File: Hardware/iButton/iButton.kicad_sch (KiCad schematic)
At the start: 29 parts, among them IC1 TSOP75338TR, J1 Conn_01x06, X1b1 PG-2.5-9.5-SM, X2b1 PG-2.5-8.0-SM, X3b1 PG-3.0-10.0-SM

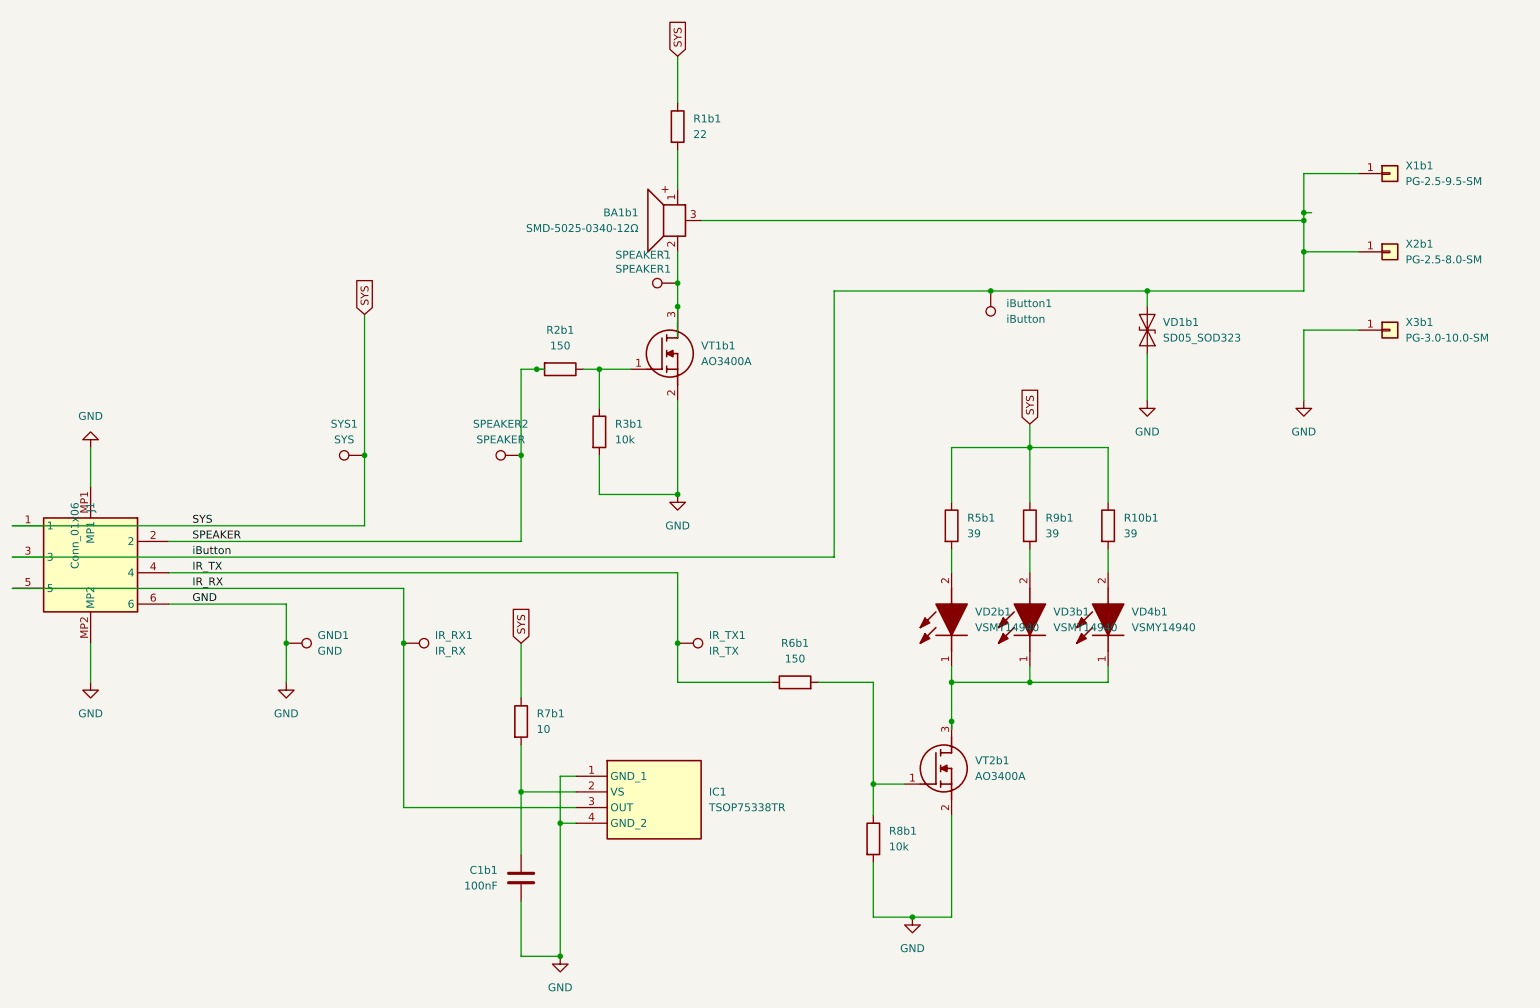
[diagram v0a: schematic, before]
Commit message: PCB: Re layout the iBTN board
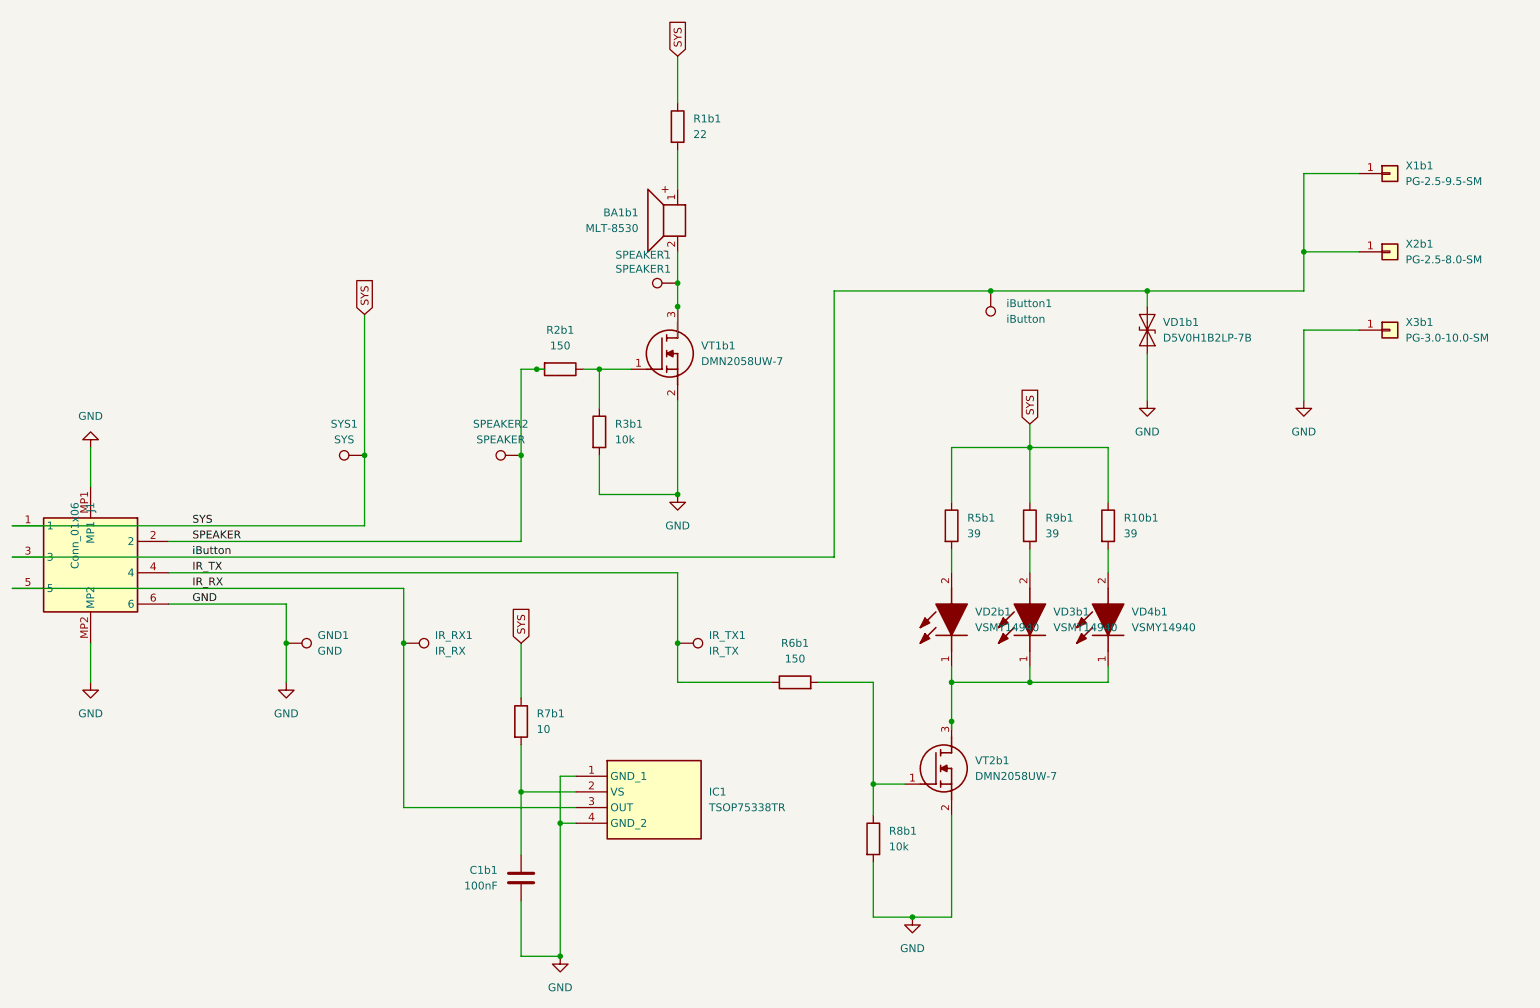
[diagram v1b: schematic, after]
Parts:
- BA1b1: value SMD-5025-0340-12Ω -> MLT-8530; footprint Library:BUZ-SMD_3P-L5.0-W5.0-BL -> Library:MLT8530
- GND1, IR_RX1, IR_TX1, SPEAKER1, SPEAKER2, SYS1, iButton1: footprint TestPoint:TestPoint_Pad_1.0x1.0mm -> TestPoint:TestPoint_Pad_D1.0mm
- VD1b1: value SD05_SOD323 -> D5V0H1B2LP-7B; footprint Diode_SMD:D_SOD-323 -> Library:D5V0H1B2LP7B
- VT1b1, VT2b1: value AO3400A -> DMN2058UW-7; footprint SOT95P280X125-3N -> Library:SOT65P210X110-3N
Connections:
- net iButton: no longer BA1b1.3
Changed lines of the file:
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@@
 	)
 	(junction
-		(at 228.6 50.8)
-		(diameter 0)
-		(color 0 0 0 0)
-	)
-	(junction
 		(at 107.95 149.86)
 		(diameter 0)
@@
 	)
 	(junction
-		(at 228.6 52.07)
-		(diameter 0)
-		(color 0 0 0 0)
-	)
-	(junction
 		(at 127 96.52)
 		(diameter 0)
@@
 	(wire
 		(pts
-			(xy 228.6 57.15) (xy 228.6 52.07)
+			(xy 228.6 44.45) (xy 228.6 57.15)
 		)
 		(stroke
@@
 	(wire
 		(pts
-			(xy 130.81 52.07) (xy 228.6 52.07)
-		)
-		(stroke
-			(width 0)
-			(type default)
-		)
-	)
-	(wire
-		(pts
 			(xy 101.6 162.56) (xy 101.6 171.45)
 		)
@@
 	(wire
 		(pts
-			(xy 228.6 52.07) (xy 228.6 50.8)
-		)
-		(stroke
-			(width 0)
-			(type default)
-		)
-	)
-	(wire
-		(pts
 			(xy 63.5 120.65) (xy 63.5 114.3)
 		)
@@
 	(wire
 		(pts
-			(xy 229.87 50.8) (xy 228.6 50.8)
-		)
-		(stroke
-			(width 0)
-			(type default)
-		)
-	)
-	(wire
-		(pts
 			(xy 101.6 137.16) (xy 101.6 144.78)
 		)
@@
 	(wire
 		(pts
-			(xy 228.6 44.45) (xy 228.6 50.8)
-		)
-		(stroke
-			(width 0)
-			(type default)
-		)
-	)
-	(wire
-		(pts
 			(xy 127 127) (xy 142.24 127)
 		)
@@
 			)
 		)
-		(property "Footprint" "TestPoint:TestPoint_Pad_1.0x1.0mm"
+		(property "Footprint" "TestPoint:TestPoint_Pad_D1.0mm"
 			(at 63.5 125.73 0)
 			(effects
@@
 			)
 		)
-		(property "Footprint" "TestPoint:TestPoint_Pad_1.0x1.0mm"
+		(property "Footprint" "TestPoint:TestPoint_Pad_D1.0mm"
 			(at 172.72 63.5 0)
 			(effects
@@
 			)
 		)
-		(property "Footprint" "TestPoint:TestPoint_Pad_1.0x1.0mm"
+		(property "Footprint" "TestPoint:TestPoint_Pad_D1.0mm"
 			(at 127 57.15 0)
 			(effects
@@
 			)
 		)
-		(property "Value" "SD05_SOD323"
+		(property "Value" "D5V0H1B2LP-7B"
 			(at 205.74 71.1199 90)
 			(effects
@@
 			)
 		)
-		(property "Footprint" "Diode_SMD:D_SOD-323"
+		(property "Footprint" "Library:D5V0H1B2LP7B"
 			(at 208.28 69.85 0)
 			(effects
@@
 			)
 		)
-		(property "Footprint" "TestPoint:TestPoint_Pad_1.0x1.0mm"
+		(property "Footprint" "TestPoint:TestPoint_Pad_D1.0mm"
 			(at 101.6 85.09 0)
 			(effects
@@
 			)
 		)
-		(property "Value" "AO3400A"
+		(property "Value" "DMN2058UW-7"
 			(at 130.81 74.9299 0)
 			(effects
@@
 			)
 		)
-		(property "Footprint" "SOT95P280X125-3N"
+		(property "Footprint" "Library:SOT65P210X110-3N"
 			(at 130.81 174.93 0)
 			(effects
@@
 			)
 		)
-		(property "Value" "AO3400A"
+		(property "Value" "DMN2058UW-7"
 			(at 175.26 142.2399 0)
 			(effects
@@
 			)
 		)
-		(property "Footprint" "SOT95P280X125-3N"
+		(property "Footprint" "Library:SOT65P210X110-3N"
 			(at 175.26 242.24 0)
 			(effects
@@
 			)
 		)
-		(property "Footprint" "TestPoint:TestPoint_Pad_1.0x1.0mm"
+		(property "Footprint" "TestPoint:TestPoint_Pad_D1.0mm"
 			(at 82.55 125.73 0)
 			(effects
@@
 			)
 		)
-		(property "Footprint" "TestPoint:TestPoint_Pad_1.0x1.0mm"
+		(property "Footprint" "TestPoint:TestPoint_Pad_D1.0mm"
 			(at 127 125.73 0)
 			(effects
@@
 			)
 		)
-		(property "Value" "SMD-5025-0340-12Ω"
+		(property "Value" "MLT-8530"
 			(at 120.65 53.3399 0)
 			(effects
@@
 			)
 		)
-		(property "Footprint" "Library:BUZ-SMD_3P-L5.0-W5.0-BL"
+		(property "Footprint" "Library:MLT8530"
 			(at 125.73 55.88 0)
 			(effects
@@
 		(pin "2"
 		)
-		(pin "3"
-		)
 		(instances
 			(project "iButton"
@@
 			)
 		)
-		(property "Footprint" "TestPoint:TestPoint_Pad_1.0x1.0mm"
+		(property "Footprint" "TestPoint:TestPoint_Pad_D1.0mm"
 			(at 76.2 85.09 0)
 			(effects
